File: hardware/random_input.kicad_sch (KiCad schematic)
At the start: 32 parts, among them J1 FS, J2 FS_G, J3 In_G, J4 Out_G, J5 -, J6 In, J7 Out, J8 +, Q1 NPN Ge, Q2 NPN Ge

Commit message: Address issues found in v0.01 hardware
 - Move all potentiometers to back copper layer (they were reversed)
 - cosmetic/usability updates
 - adjust value of Q2 trimpot to allow correct biasing
 - swap FS and FS_G wires
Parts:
- POT1: value In_Volume (A100K) -> A100K; Label (none) -> Input Volume
- POT2: value Fuzz(B1K) -> B1K; Field4 (none) -> Fuzz
- POT3: value Volume (A250K) -> A250K; Label (none) -> Volume
- TP1: value Q1 bias -> Q1 Bias
- TP2: value Q2 bias -> Q2 Bias
- TRIM1: value Q1_BIAS_100K -> 100K; Label (none) -> Q1 Bias
- TRIM2: value Q2_BIAS_20K -> 50K; Label (none) -> Q2 Bias
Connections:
- net 9V: now also D2.2 (A)
- net DC_SHIELD: no longer D2.2 (A)
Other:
- moved on the sheet: D1, D2
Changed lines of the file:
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@@
     (title "Random Input Fuzz Effect (Based on Fuzz Face)")
     (date "2023-02-21")
-    (rev "v0.01")
+    (rev "v0.1")
   )
   (junction (at 66.04 34.29) (diameter 0) (color 0 0 0 0)
@@
   (junction (at 109.22 124.46) (diameter 0) (color 0 0 0 0)
   )
-  (junction (at 29.21 118.11) (diameter 0) (color 0 0 0 0)
-  )
   (junction (at 30.48 45.72) (diameter 0) (color 0 0 0 0)
   )
@@
   (junction (at 88.9 34.29) (diameter 0) (color 0 0 0 0)
   )
+  (junction (at 36.83 118.11) (diameter 0) (color 0 0 0 0)
+  )
   (junction (at 109.22 143.51) (diameter 0) (color 0 0 0 0)
   )
@@
     (stroke (width 0) (type default))
   )
-  (wire (pts (xy 17.78 118.11) (xy 29.21 118.11))
+  (wire (pts (xy 17.78 118.11) (xy 26.67 118.11))
     (stroke (width 0) (type default))
   )
@@
     (stroke (width 0) (type default))
   )
-  (wire (pts (xy 39.37 118.11) (xy 41.91 118.11))
-    (stroke (width 0) (type default))
-  )
   (wire (pts (xy 88.9 151.13) (xy 88.9 153.67))
     (stroke (width 0) (type default))
@@
     (stroke (width 0) (type default))
   )
-  (wire (pts (xy 29.21 118.11) (xy 29.21 105.41))
-    (stroke (width 0) (type default))
-  )
   (wire (pts (xy 95.25 85.09) (xy 95.25 86.36))
     (stroke (width 0) (type default))
@@
     (stroke (width 0) (type default))
   )
-  (wire (pts (xy 29.21 105.41) (xy 31.75 105.41))
-    (stroke (width 0) (type default))
-  )
   (wire (pts (xy 99.06 167.64) (xy 109.22 167.64))
     (stroke (width 0) (type default))
@@
     (stroke (width 0) (type default))
   )
+  (wire (pts (xy 38.1 105.41) (xy 36.83 105.41))
+    (stroke (width 0) (type default))
+  )
   (wire (pts (xy 109.22 167.64) (xy 118.11 167.64))
     (stroke (width 0) (type default))
@@
     (stroke (width 0) (type default))
   )
+  (wire (pts (xy 34.29 118.11) (xy 36.83 118.11))
+    (stroke (width 0) (type default))
+  )
   (wire (pts (xy 69.85 34.29) (xy 69.85 29.21))
     (stroke (width 0) (type default))
@@
     (stroke (width 0) (type default))
   )
+  (wire (pts (xy 36.83 118.11) (xy 41.91 118.11))
+    (stroke (width 0) (type default))
+  )
   (wire (pts (xy 30.48 45.72) (xy 17.78 45.72))
     (stroke (width 0) (type default))
@@
     (stroke (width 0) (type default))
   )
-  (wire (pts (xy 39.37 105.41) (xy 46.99 105.41))
-    (stroke (width 0) (type default))
-  )
-  (wire (pts (xy 29.21 118.11) (xy 31.75 118.11))
-    (stroke (width 0) (type default))
-  )
   (wire (pts (xy 73.66 21.59) (xy 66.04 21.59))
     (stroke (width 0) (type default))
   )
+  (wire (pts (xy 36.83 105.41) (xy 36.83 118.11))
+    (stroke (width 0) (type default))
+  )
   (wire (pts (xy 109.22 124.46) (xy 109.22 106.68))
     (stroke (width 0) (type default))
@@
   )
   (wire (pts (xy 88.9 143.51) (xy 109.22 143.51))
+    (stroke (width 0) (type default))
+  )
+  (wire (pts (xy 45.72 105.41) (xy 46.99 105.41))
     (stroke (width 0) (type default))
   )
@@
       (effects (font (size 1.27 1.27)) (justify right))
     )
-    (property "Value" "Q1_BIAS_100K" (at 64.77 30.48 0)
+    (property "Value" "100K" (at 64.77 30.48 0)
       (effects (font (size 1.27 1.27)) (justify right))
     )
@@
       (effects (font (size 1.27 1.27)) hide)
     )
+    (property "Label" "Q1 Bias" (at 55.88 29.21 0)
+      (effects (font (size 1.27 1.27)))
+    )
     (pin "1")
     (pin "2")
@@
       (effects (font (size 1.27 1.27)))
     )
-    (property "Value" "Fuzz(B1K)" (at 82.55 73.66 0)
+    (property "Value" "B1K" (at 85.09 72.39 0)
       (effects (font (size 1.27 1.27)))
     )
@@
     (property "Datasheet" "~" (at 88.9 73.66 0)
       (effects (font (size 1.27 1.27)) hide)
+    )
+    (property "Field4" "Fuzz" (at 85.09 74.93 0)
+      (effects (font (size 1.27 1.27)))
     )
     (pin "1")
@@
       (effects (font (size 1.27 1.27)) (justify right))
     )
-    (property "Value" "Q2_BIAS_20K" (at 87.63 30.48 0)
+    (property "Value" "50K" (at 87.63 30.48 0)
       (effects (font (size 1.27 1.27)) (justify right))
     )
@@
     (property "Datasheet" "~" (at 88.9 29.21 0)
       (effects (font (size 1.27 1.27)) hide)
+    )
+    (property "Label" "Q2 Bias" (at 78.74 29.21 0)
+      (effects (font (size 1.27 1.27)))
     )
     (pin "1")
@@
     )
   )
-  (symbol (lib_id "Device:D") (at 35.56 118.11 180) (unit 1)
-    (in_bom yes) (on_board yes) (dnp no)
-    (property "Reference" "D1" (at 35.56 115.57 0)
-      (effects (font (size 1.27 1.27)))
-    )
-    (property "Value" "1N5817" (at 35.56 120.65 0)
-      (effects (font (size 1.27 1.27)))
-    )
-    (property "Footprint" "Diode_THT:D_DO-35_SOD27_P7.62mm_Horizontal" (at 35.56 118.11 0)
-      (effects (font (size 1.27 1.27)) hide)
-    )
-    (property "Datasheet" "~" (at 35.56 118.11 0)
-      (effects (font (size 1.27 1.27)) hide)
-    )
-    (property "Sim.Device" "D" (at 35.56 118.11 0)
-      (effects (font (size 1.27 1.27)) hide)
-    )
-    (property "Sim.Pins" "1=K 2=A" (at 35.56 118.11 0)
+  (symbol (lib_id "Device:D") (at 30.48 118.11 180) (unit 1)
+    (in_bom yes) (on_board yes) (dnp no)
+    (property "Reference" "D1" (at 30.48 115.57 0)
+      (effects (font (size 1.27 1.27)))
+    )
+    (property "Value" "1N5817" (at 30.48 120.65 0)
+      (effects (font (size 1.27 1.27)))
+    )
+    (property "Footprint" "Diode_THT:D_DO-35_SOD27_P7.62mm_Horizontal" (at 30.48 118.11 0)
+      (effects (font (size 1.27 1.27)) hide)
+    )
+    (property "Datasheet" "~" (at 30.48 118.11 0)
+      (effects (font (size 1.27 1.27)) hide)
+    )
+    (property "Sim.Device" "D" (at 30.48 118.11 0)
+      (effects (font (size 1.27 1.27)) hide)
+    )
+    (property "Sim.Pins" "1=K 2=A" (at 30.48 118.11 0)
       (effects (font (size 1.27 1.27)) hide)
     )
@@
       (effects (font (size 1.27 1.27)))
     )
-    (property "Value" "Volume (A250K)" (at 102.87 30.48 0)
+    (property "Value" "A250K" (at 106.68 27.94 0)
       (effects (font (size 1.27 1.27)))
     )
@@
       (effects (font (size 1.27 1.27)) hide)
     )
+    (property "Label" "Volume" (at 106.68 30.48 0)
+      (effects (font (size 1.27 1.27)))
+    )
     (pin "1")
     (pin "2")
@@
       (effects (font (size 1.27 1.27)))
     )
-    (property "Value" "Q2 bias" (at 85.09 40.64 90)
+    (property "Value" "Q2 Bias" (at 85.09 40.64 90)
       (effects (font (size 1.27 1.27)))
     )
@@
       (effects (font (size 1.27 1.27)))
     )
-    (property "Value" "In_Volume (A100K)" (at 38.1 55.88 90)
+    (property "Value" "A100K" (at 38.1 55.88 90)
       (effects (font (size 1.27 1.27)))
     )
@@
     (property "Datasheet" "~" (at 38.1 53.34 0)
       (effects (font (size 1.27 1.27)) hide)
+    )
+    (property "Label" "Input Volume" (at 38.1 58.42 90)
+      (effects (font (size 1.27 1.27)))
     )
     (pin "1")
@@
     )
   )
-  (symbol (lib_id "Device:LED") (at 35.56 105.41 180) (unit 1)
-    (in_bom yes) (on_board yes) (dnp no)
-    (property "Reference" "D2" (at 35.56 102.87 0)
-      (effects (font (size 1.27 1.27)))
-    )
-    (property "Value" "On" (at 35.56 107.95 0)
-      (effects (font (size 1.27 1.27)))
-    )
-    (property "Footprint" "LED_THT:LED_D3.0mm" (at 35.56 105.41 0)
-      (effects (font (size 1.27 1.27)) hide)
-    )
-    (property "Datasheet" "~" (at 35.56 105.41 0)
+  (symbol (lib_id "Device:LED") (at 41.91 105.41 180) (unit 1)
+    (in_bom yes) (on_board yes) (dnp no)
+    (property "Reference" "D2" (at 41.91 102.87 0)
+      (effects (font (size 1.27 1.27)))
+    )
+    (property "Value" "On" (at 41.91 107.95 0)
+      (effects (font (size 1.27 1.27)))
+    )
+    (property "Footprint" "LED_THT:LED_D3.0mm" (at 41.91 105.41 0)
+      (effects (font (size 1.27 1.27)) hide)
+    )
+    (property "Datasheet" "~" (at 41.91 105.41 0)
       (effects (font (size 1.27 1.27)) hide)
     )
@@
       (effects (font (size 1.27 1.27)))
     )
-    (property "Value" "Q1 bias" (at 69.85 40.64 90)
-      (effects (font (size 1.27 1.27)))
-    )
+    (property "Value" "Q1 Bias" (at 69.85 40.64 90)
+      (effects (font (size 1.27 1.27)))
+    )

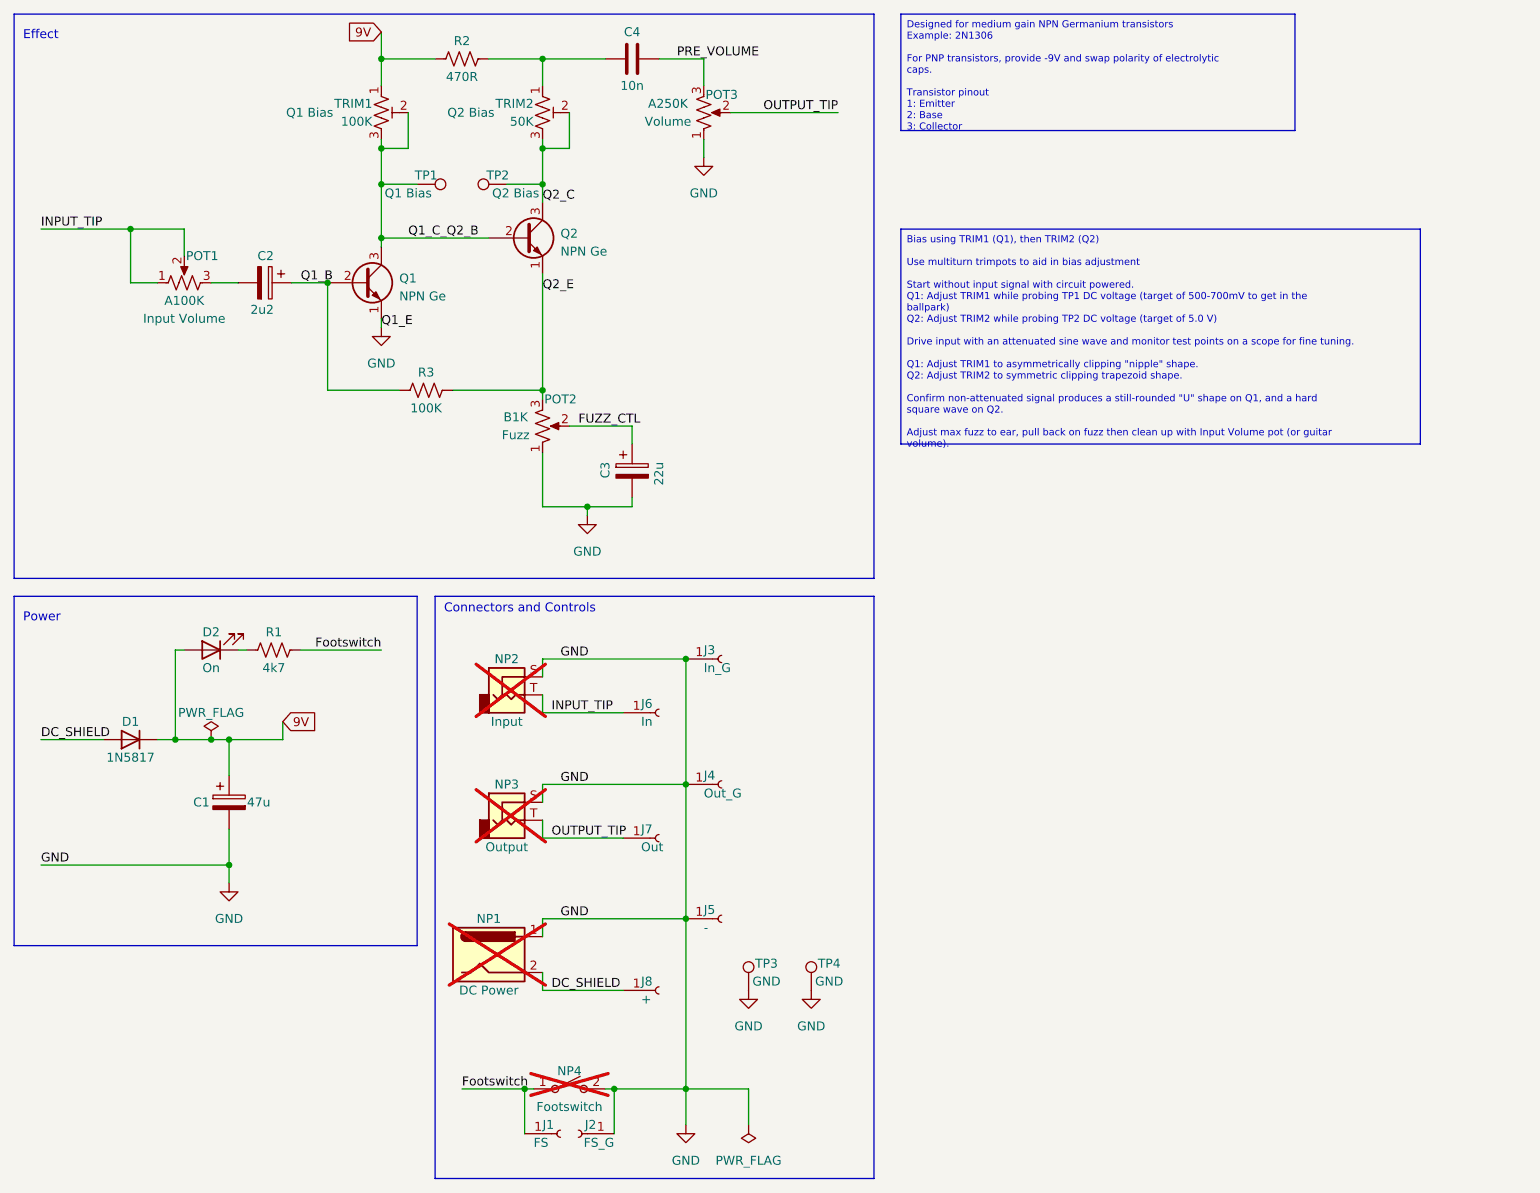
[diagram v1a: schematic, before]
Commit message: Updates for v0.2:
 - Switch from wire connectors to molex picoblade connectors
 - Increase size / ergonomics of bias testing pads to suit more probe types
 - Various cosmetic fixes
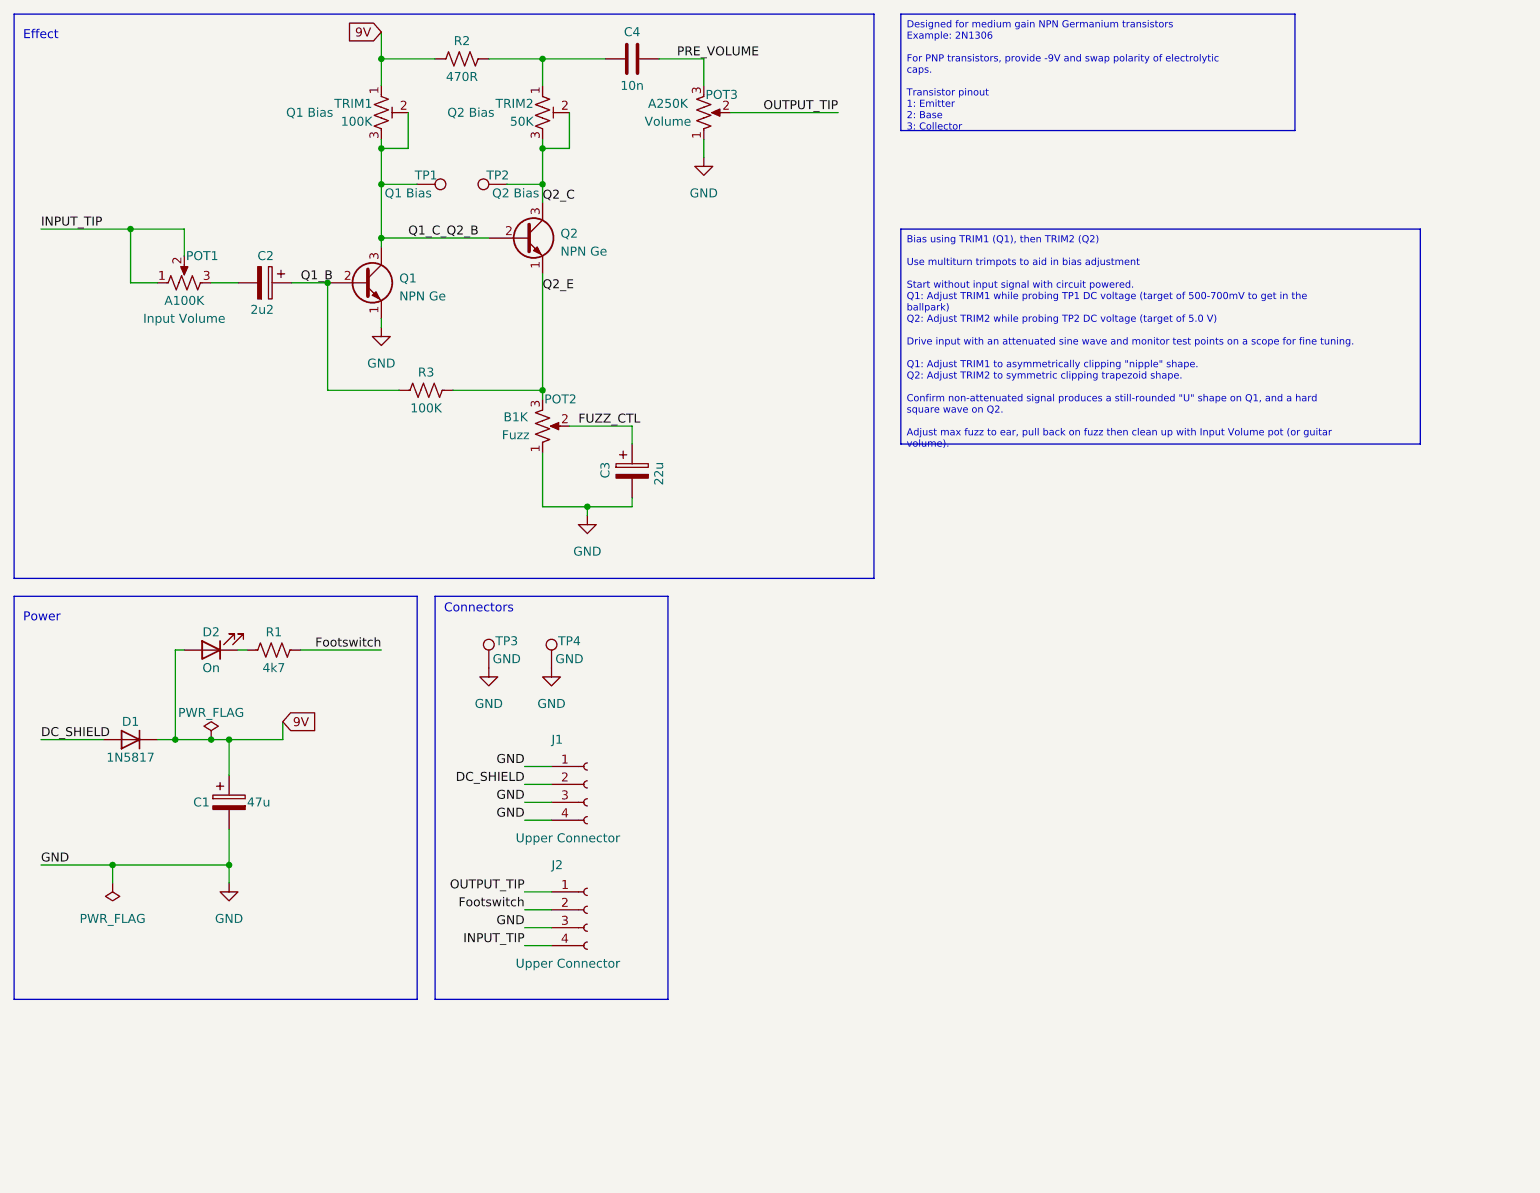
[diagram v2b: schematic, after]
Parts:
- removed J1: FS, Connector_Wire:SolderWire-0.5sqmm_1x01_D0.9mm_OD2.1mm, symbol Connector:Conn_01x01_Socket
- removed J2: FS_G, Connector_Wire:SolderWire-0.5sqmm_1x01_D0.9mm_OD2.1mm, symbol Connector:Conn_01x01_Socket
- removed J3: In_G, Connector_Wire:SolderWire-0.5sqmm_1x01_D0.9mm_OD2.1mm, symbol Connector:Conn_01x01_Socket
- removed J4: Out_G, Connector_Wire:SolderWire-0.5sqmm_1x01_D0.9mm_OD2.1mm, symbol Connector:Conn_01x01_Socket
- removed J5: -, Connector_Wire:SolderWire-0.5sqmm_1x01_D0.9mm_OD2.1mm, symbol Connector:Conn_01x01_Socket
- removed J6: In, Connector_Wire:SolderWire-0.5sqmm_1x01_D0.9mm_OD2.1mm, symbol Connector:Conn_01x01_Socket
- removed J7: Out, Connector_Wire:SolderWire-0.5sqmm_1x01_D0.9mm_OD2.1mm, symbol Connector:Conn_01x01_Socket
- removed J8: +, Connector_Wire:SolderWire-0.5sqmm_1x01_D0.9mm_OD2.1mm, symbol Connector:Conn_01x01_Socket
- removed NP1: DC Power, symbol Connector:Barrel_Jack
- removed NP2: Input, symbol Connector_Audio:AudioJack2
- removed NP3: Output, symbol Connector_Audio:AudioJack2
- removed NP4: Footswitch, symbol Switch:SW_SPST
- added J1, J2: Upper Connector, Connector_Molex:Molex_PicoBlade_53047-0410_1x04_P1.25mm_Vertical, symbol Connector:Conn_01x04_Socket
- TP1, TP2, TP3, TP4: footprint TestPoint:TestPoint_THTPad_D2.0mm_Drill1.0mm -> TestPoint:TestPoint_THTPad_2.5x2.5mm_Drill1.2mm
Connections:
- net DC_SHIELD: now also J1.2 (Pin_2)
- net Footswitch: now also J2.2 (Pin_2)
- net GND: now also J1.1 (Pin_1), J1.3 (Pin_3), J1.4 (Pin_4), J2.3 (Pin_3)
- net INPUT_TIP: now also J2.4 (Pin_4)
- net OUTPUT_TIP: now also J2.1 (Pin_1)
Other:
- note added: "Connectors"
- note removed: "Connectors and Controls"
- moved on the sheet: TP3, TP4

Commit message: Offload DC protection to "noise floor" utility PCB
 - much rerouting but otherwise functionally the same
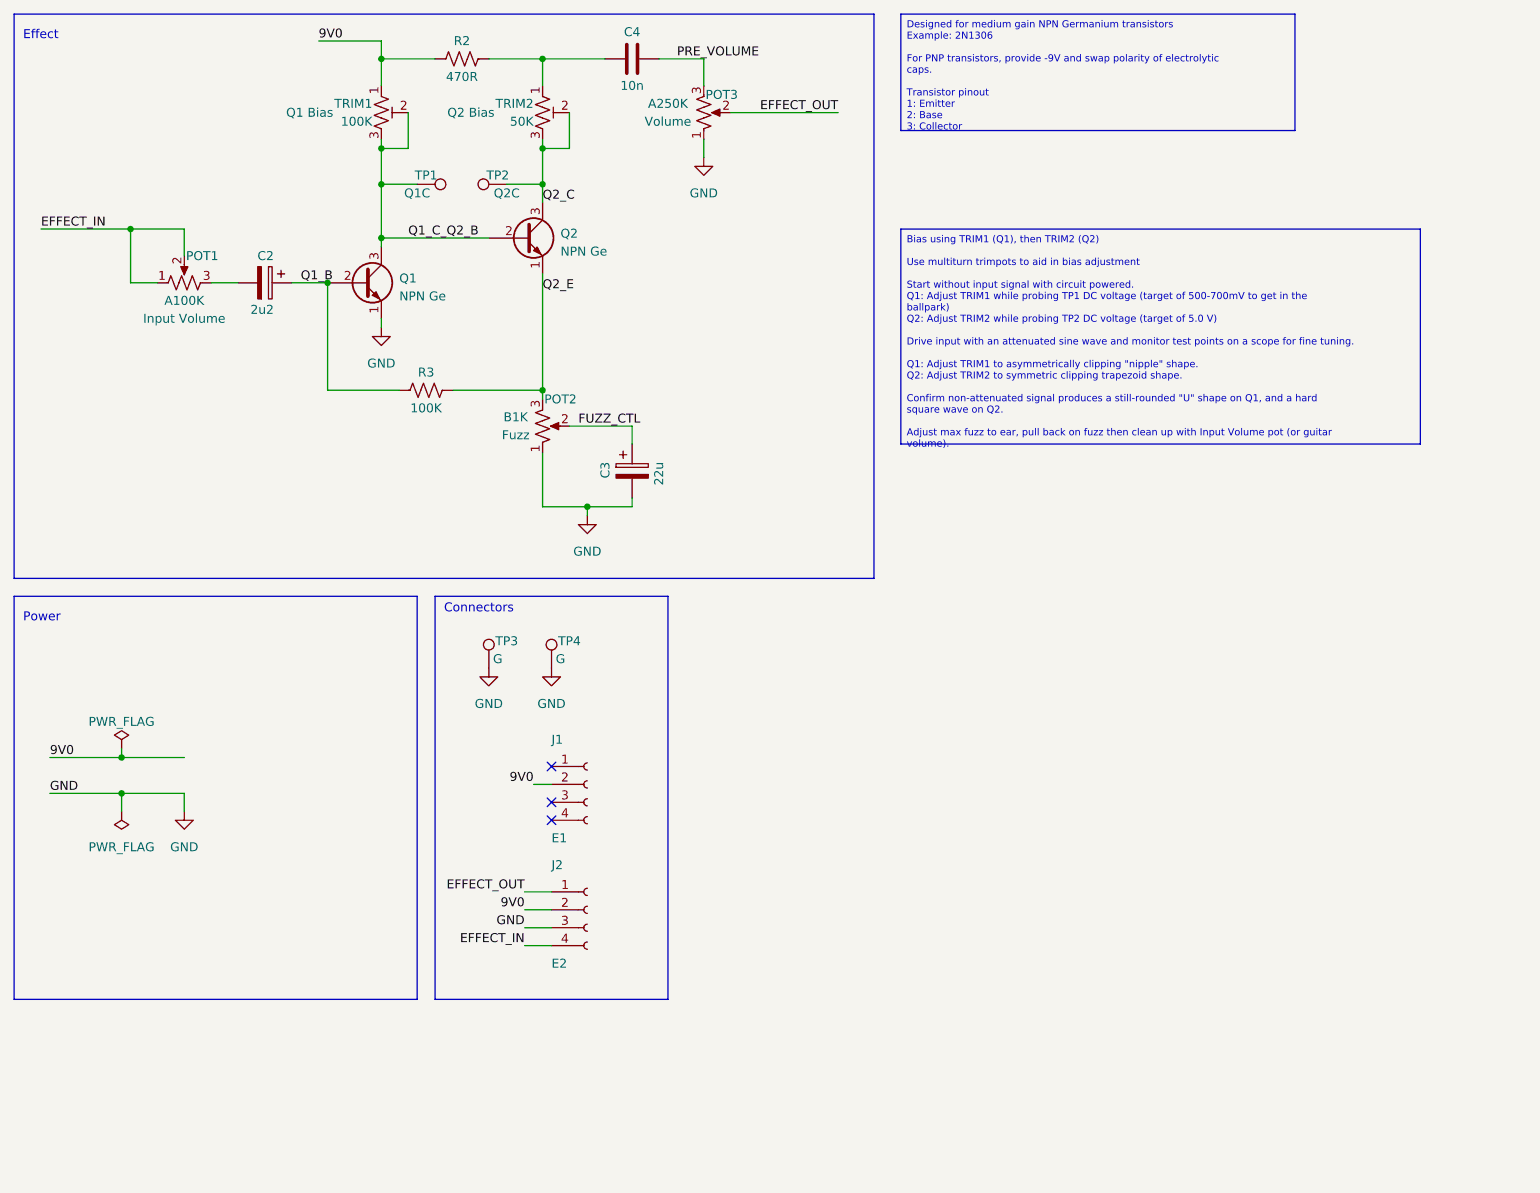
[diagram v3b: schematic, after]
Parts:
- removed C1: 47u, Capacitor_THT:CP_Radial_D5.0mm_P2.50mm, symbol Device:C_Polarized
- removed D1: 1N5817, Diode_THT:D_DO-35_SOD27_P7.62mm_Horizontal, symbol Device:D
- removed D2: On, LED_THT:LED_D3.0mm, symbol Device:LED
- removed R1: 4k7, Resistor_THT:R_Axial_DIN0207_L6.3mm_D2.5mm_P7.62mm_Horizontal, symbol Device:R_US
- J1: value Upper Connector -> E1
- J2: value Upper Connector -> E2
- TP1: value Q1 Bias -> Q1C
- TP2: value Q2 Bias -> Q2C
- TP3, TP4: value GND -> G
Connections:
- net DC_SHIELD is gone; now on net 9V0: J1.2 (Pin_2)
- net Footswitch is gone; now on net 9V0: J2.2 (Pin_2)
- net GND: no longer J1.1 (Pin_1), J1.3 (Pin_3), J1.4 (Pin_4)
- net 9V renamed 9V0
- net INPUT_TIP renamed EFFECT_IN
- net OUTPUT_TIP renamed EFFECT_OUT
- no-connect marks 0 -> 3
